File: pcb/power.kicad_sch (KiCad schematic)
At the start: 29 parts, among them Q5 AO3407A, SW3 POWER, U1 TPS2121RUXR, U2 TPS2121RUXR, U3 TPS2121RUXR, U4 74LVC1G08

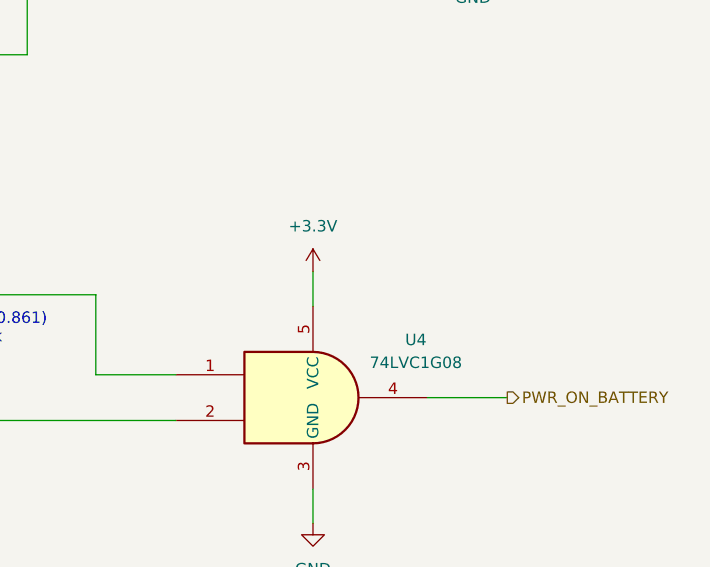
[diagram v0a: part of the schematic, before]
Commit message: Add U4 decoupling cap, source U15 MPN, improve GND/GNDREF visual distinction
- Add local decoupling capacitor to U4 (74LVC1G08) VCC/GND
- Add missing Manf/MPN/LCSC Part# to U15 (PCA9555PWR, TI, C2864778) found
  during a full net-trace design review
- Color all GNDREF net wires in battery_18650_input.kicad_sch orange to
  make the intentional GND/GNDREF current-sense split (bridged only by
  R13) visually obvious on the canvas, not just from the net name
- Add a schematic text note at R13 documenting the split for reviewers
  without access to CLAUDE.md

Co-Authored-By: Claude Sonnet 5 <noreply@anthropic.com>
Claude-Session: https://claude.ai/code/session_01LhLkuH6sQ5GbUZ61bG7p2h
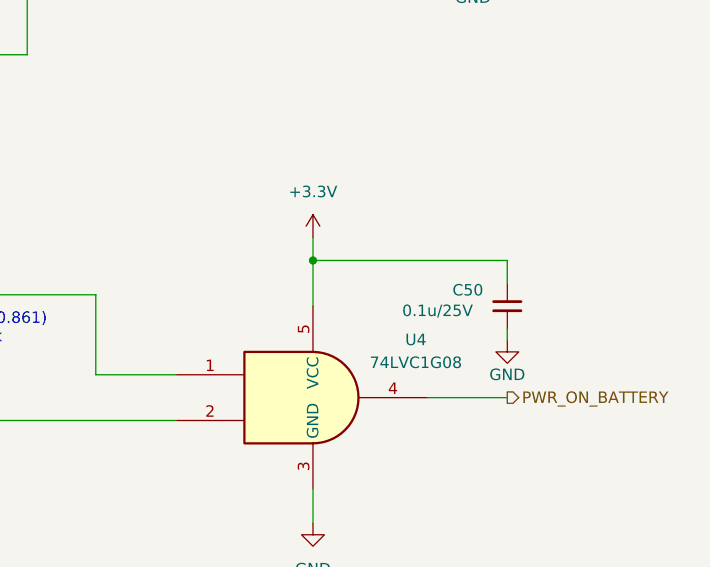
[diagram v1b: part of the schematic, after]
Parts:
- added C50: 0.1u/25V, Capacitor_SMD:C_0603_1608Metric, symbol Device:C_Small
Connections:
- net +3.3V: now also C50.1
- net GND: now also C50.2

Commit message: Wire SD card interface, fix R29/Q6/Q7 sourcing, localize datasheets project-wide
- SD card (Card1, Molex 472192001) wired to the FSPI (SPI2) peripheral:
  IO10/FSPICS0->CS, IO11/FSPID->MOSI, IO12/FSPICLK->SCLK, IO13/FSPIQ->MISO;
  shield/mounting tabs renamed SHLD and grounded; local decoupling cap added
- R29 was silently a 10k YAGEO part (RC0603FR-0710KL/C98220) sitting under a
  1M designator -- corrected to the real 1M part (RC0603FR-071ML/C105578),
  matching this rail's documented VRAW soft-latch bleed design intent
- Q6, Q7 (BSS138): added missing Manf/MPN/LCSC Part# (onsemi BSS138LT1G,
  C82045)
- C32/C36: normalized Value strings; fixed C36's Datasheet, which pointed to
  a different capacitor's PDF entirely
- Localized every remaining component's Datasheet field to a project-local
  path across all 8 schematic sheets (was a live remote URL before), per
  the new datasheet-localization task; caught and rejected a wrong-language
  and a wrong-manufacturer-clone source along the way (U8, U14, U15, Y2)
- Fixed 4 datasheet fields (Q1, D1, U6, U7) that had reverted from their
  already-localized paths back to remote URLs, apparently from a native
  KiCad symbol-library resync picking up stale library-level defaults

Co-Authored-By: Claude Sonnet 5 <noreply@anthropic.com>
Claude-Session: https://claude.ai/code/session_01LhLkuH6sQ5GbUZ61bG7p2h
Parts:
- U1, U2, U3: LCSC Part (none) -> C485916; Manufacturer (none) -> TI
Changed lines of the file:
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@@
 			)
 		)
-		(property "Description" "CAP CER 10nF 50V C0G 0603"
+		(property "Description" "Unpolarized capacitor, small symbol"
 			(at 138.43 144.78 0)
 			(hide yes)
@@
 			)
 		)
-		(property "Description" "RES 30.1kΩ ±1% 100mW 0603"
+		(property "Description" "Resistor, US symbol"
 			(at 129.54 186.69 0)
 			(hide yes)
@@
 			)
 		)
-		(property "Datasheet" "https://lcsc.com/product-detail/New-Arrivals_Texas-Instruments-Texas-Instruments-TPS2121RUXR_C485916.html"
+		(property "Datasheet" "${KIPRJMOD}/libs/kicad_gx_library/datasheets/Texas_Instruments/TPS2121RUXR.pdf"
 			(at 127 64.77 0)
 			(hide yes)
@@
 			)
 		)
+		(property "Manufacturer" "TI"
+			(at 127 67.31 0)
+			(hide yes)
+			(show_name no)
+			(do_not_autoplace no)
+			(effects
+				(font
+					(size 1.27 1.27)
+				)
+			)
+		)
+		(property "LCSC Part" "C485916"
+			(at 127 72.39 0)
+			(hide yes)
+			(show_name no)
+			(do_not_autoplace no)
+			(effects
+				(font
+					(size 1.27 1.27)
+				)
+			)
+		)
 		(pin "9"
 		)
@@
 			)
 		)
-		(property "Description" "https://www.lcsc.com/datasheet/C98220.pdf"
+		(property "Description" "Resistor, US symbol"
 			(at 184.15 55.88 0)
 			(hide yes)
@@
 			)
 		)
-		(property "Description" "CAP CER 100nF 50V X7R 0603"
+		(property "Description" "Unpolarized capacitor, small symbol"
 			(at 226.06 74.93 0)
 			(hide yes)
@@
 			)
 		)
-		(property "Datasheet" "https://www.lcsc.com/datasheet/C15155.pdf"
+		(property "Datasheet" "http://www.aosmd.com/pdfs/datasheet/AO3401A.pdf"
 			(at 172.72 62.23 0)
 			(hide yes)
@@
 			)
 		)
-		(property "Description" "MOSFET P-CH 30V 4.3A SOT-23"
+		(property "Description" "-4.0A Id, -30V Vds, P-Channel MOSFET, SOT-23"
 			(at 177.8 66.04 0)
 			(hide yes)
@@
 			)
 		)
-		(property "Description" "CAP CER 10nF 50V C0G 0603"
+		(property "Description" "Unpolarized capacitor, small symbol"
 			(at 120.65 196.85 0)
 			(hide yes)
@@
 			)
 		)
-		(property "Datasheet" "https://www.lcsc.com/datasheet/C7666.pdf"
+		(property "Datasheet" "https://www.ti.com/lit/ds/symlink/sn74lvc1g08.pdf"
 			(at 207.01 135.89 0)
 			(hide yes)
@@
 			)
 		)
-		(property "Description" "Single 2-Input Positive-AND Gate"
+		(property "Description" "Single AND Gate, Low-Voltage CMOS"
 			(at 207.01 135.89 0)
 			(hide yes)
@@
 			)
 		)
-		(property "Description" "CAP CER 100nF 50V X7R 0603"
+		(property "Description" "Unpolarized capacitor, small symbol"
 			(at 228.6 135.89 0)
 			(hide yes)
@@
 			)
 		)
-		(property "Description" "RES 30.1kΩ ±1% 100mW 0603"
+		(property "Description" "Resistor, US symbol"
 			(at 151.13 60.96 0)
 			(hide yes)
@@
 			)
 		)
-		(property "Description" "CAP CER 10nF 50V C0G 0603"
+		(property "Description" "Unpolarized capacitor, small symbol"
 			(at 142.24 71.12 0)
 			(hide yes)
@@
 			)
 		)
-		(property "Datasheet" "https://lcsc.com/product-detail/New-Arrivals_Texas-Instruments-Texas-Instruments-TPS2121RUXR_C485916.html"
+		(property "Datasheet" "${KIPRJMOD}/libs/kicad_gx_library/datasheets/Texas_Instruments/TPS2121RUXR.pdf"
 			(at 123.19 138.43 0)
 			(hide yes)
@@
 			)
 		)
+		(property "Manufacturer" "TI"
+			(at 123.19 140.97 0)
+			(hide yes)
+			(show_name no)
+			(do_not_autoplace no)
+			(effects
+				(font
+					(size 1.27 1.27)
+				)
+			)
+		)
+		(property "LCSC Part" "C485916"
+			(at 123.19 146.05 0)
+			(hide yes)
+			(show_name no)
+			(do_not_autoplace no)
+			(effects
+				(font
+					(size 1.27 1.27)
+				)
+			)
+		)
 		(pin "9"
 		)
@@
 			)
 		)
-		(property "Description" "RES 80.6kΩ ±0.1% 100mW 0603"
+		(property "Description" "Resistor, US symbol"
 			(at 147.32 134.62 0)
 			(hide yes)
@@
 			)
 		)
-		(property "Datasheet" "https://lcsc.com/product-detail/New-Arrivals_Texas-Instruments-Texas-Instruments-TPS2121RUXR_C485916.html"
+		(property "Datasheet" "${KIPRJMOD}/libs/kicad_gx_library/datasheets/Texas_Instruments/TPS2121RUXR.pdf"
 			(at 105.41 190.5 0)
 			(hide yes)
@@
 			)
 		)
+		(property "Manufacturer" "TI"
+			(at 105.41 193.04 0)
+			(hide yes)
+			(show_name no)
+			(do_not_autoplace no)
+			(effects
+				(font
+					(size 1.27 1.27)
+				)
+			)
+		)
+		(property "LCSC Part" "C485916"
+			(at 105.41 198.12 0)
+			(hide yes)
+			(show_name no)
+			(do_not_autoplace no)
+			(effects
+				(font
+					(size 1.27 1.27)
+				)
+			)
+		)
 		(pin "9"
 		)
@@
 			)
 		)
-		(property "Description" "SWITCH TACTILE SPST 250gf SMD"
+		(property "Description" "Push button switch, generic, two pins"
 			(at 215.9 66.04 0)
 			(hide yes)
